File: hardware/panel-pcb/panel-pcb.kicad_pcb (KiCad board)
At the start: 4 copper layers, 135.5 x 127 mm, 131 parts, among them J1 USB_C_Receptacle_USB2.0_16P, J10 RS-485 OUT, J11 12V_OUT, J2 SWD, J3 FSR North, J4 FSR East, J5 12V_IN, J6 FSR South, J7 FSR West, J8 RS-485 IN, J9 INT OUT, SW1 PANEL_ID, SW2 BOOTSEL, SW3 RS-485 Termination, U1 RP2040, U2 THVD1419, U3 W25Q32JV, U4 SN74AHCT125, U5 AMS1117-5.0, U6 AP7361C-33ER-13, U7 USBLC6-2SC6, X1 12MHz

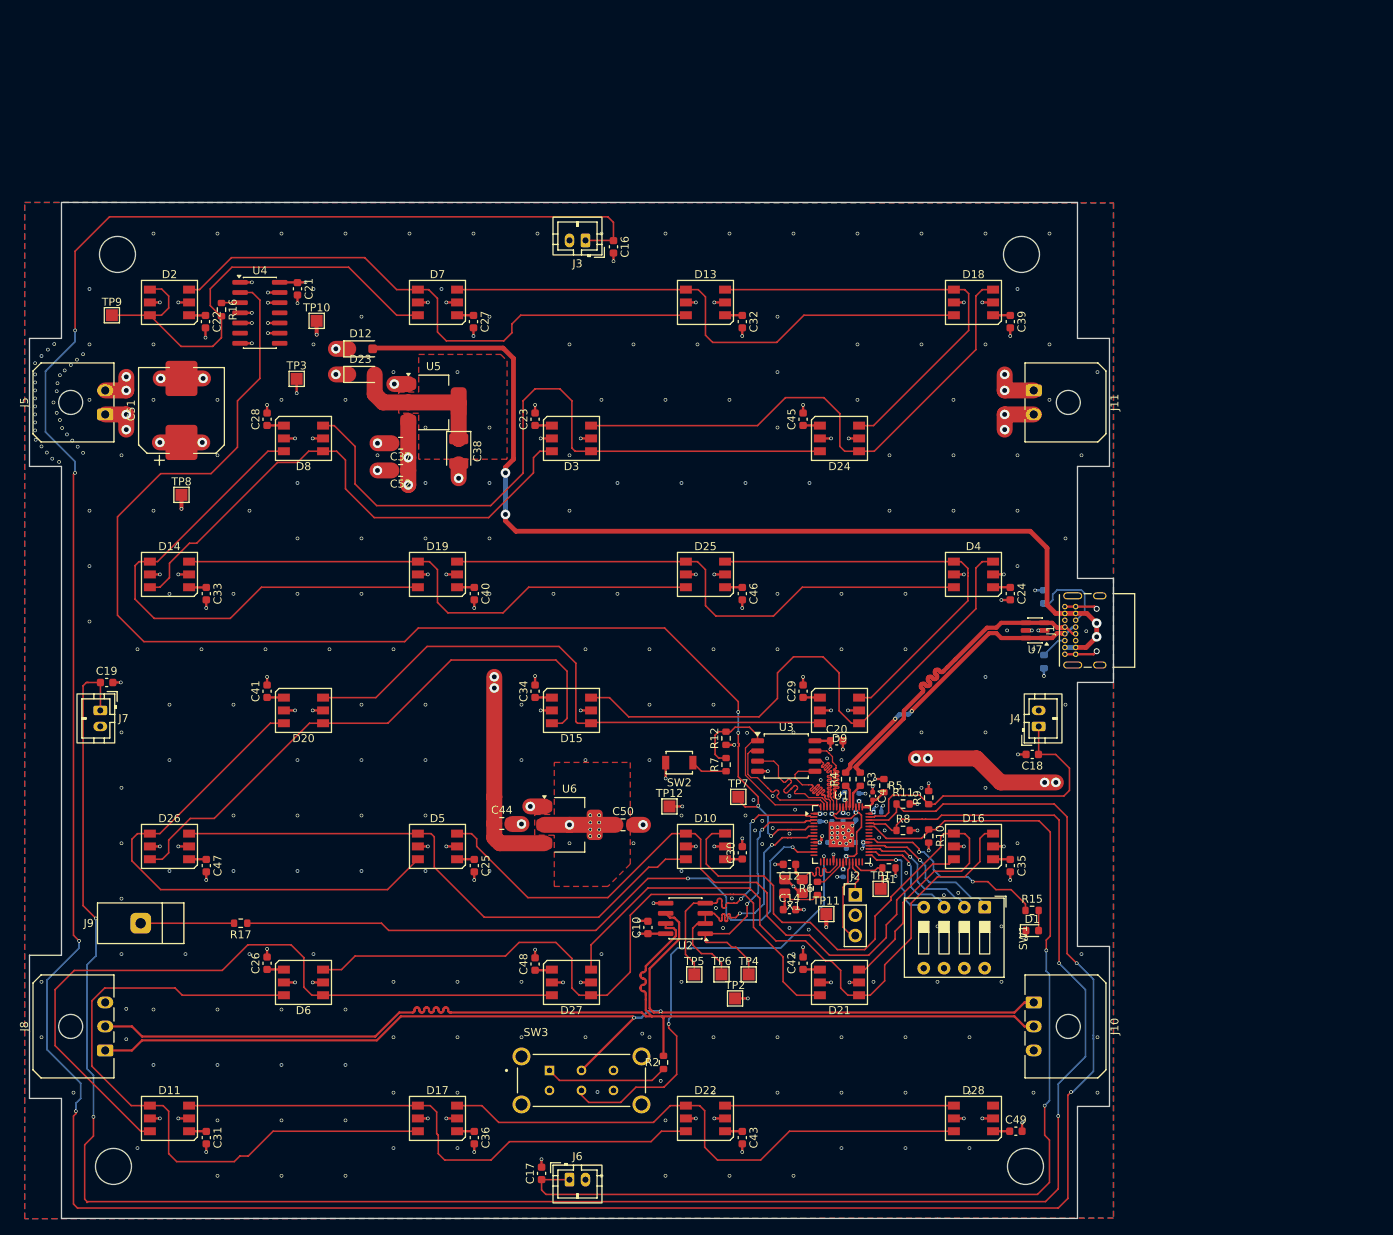
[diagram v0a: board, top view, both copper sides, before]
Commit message: Panel PCB: silkscreen positioning pass, verified ERC/DRC exclusions, page settings
- Reposition reference/value silkscreen across the board.
- Fix J1 B1/B12 starved thermal spokes.
- Save C51's edited electrolytic footprint into panel-pcb.pretty as
  CP_Elec_10x10.5_RVT1E471M and re-associate.
- Exclude verified-benign warnings: 25 lib_footprint_mismatch DRC
  false positives (rotation-correlated, content identical to library)
  and lib_symbol_mismatch ERC noise (cached flattened copies of
  derived library symbols, pins verified identical).
- Page settings: A3 -> A4 landscape, title block date/rev refreshed,
  stale mounting-hole placeholder comment removed.

Still pending before fab: silkscreen additions (name/rev/logos/JLC
order-number placeholder), final gerber export.
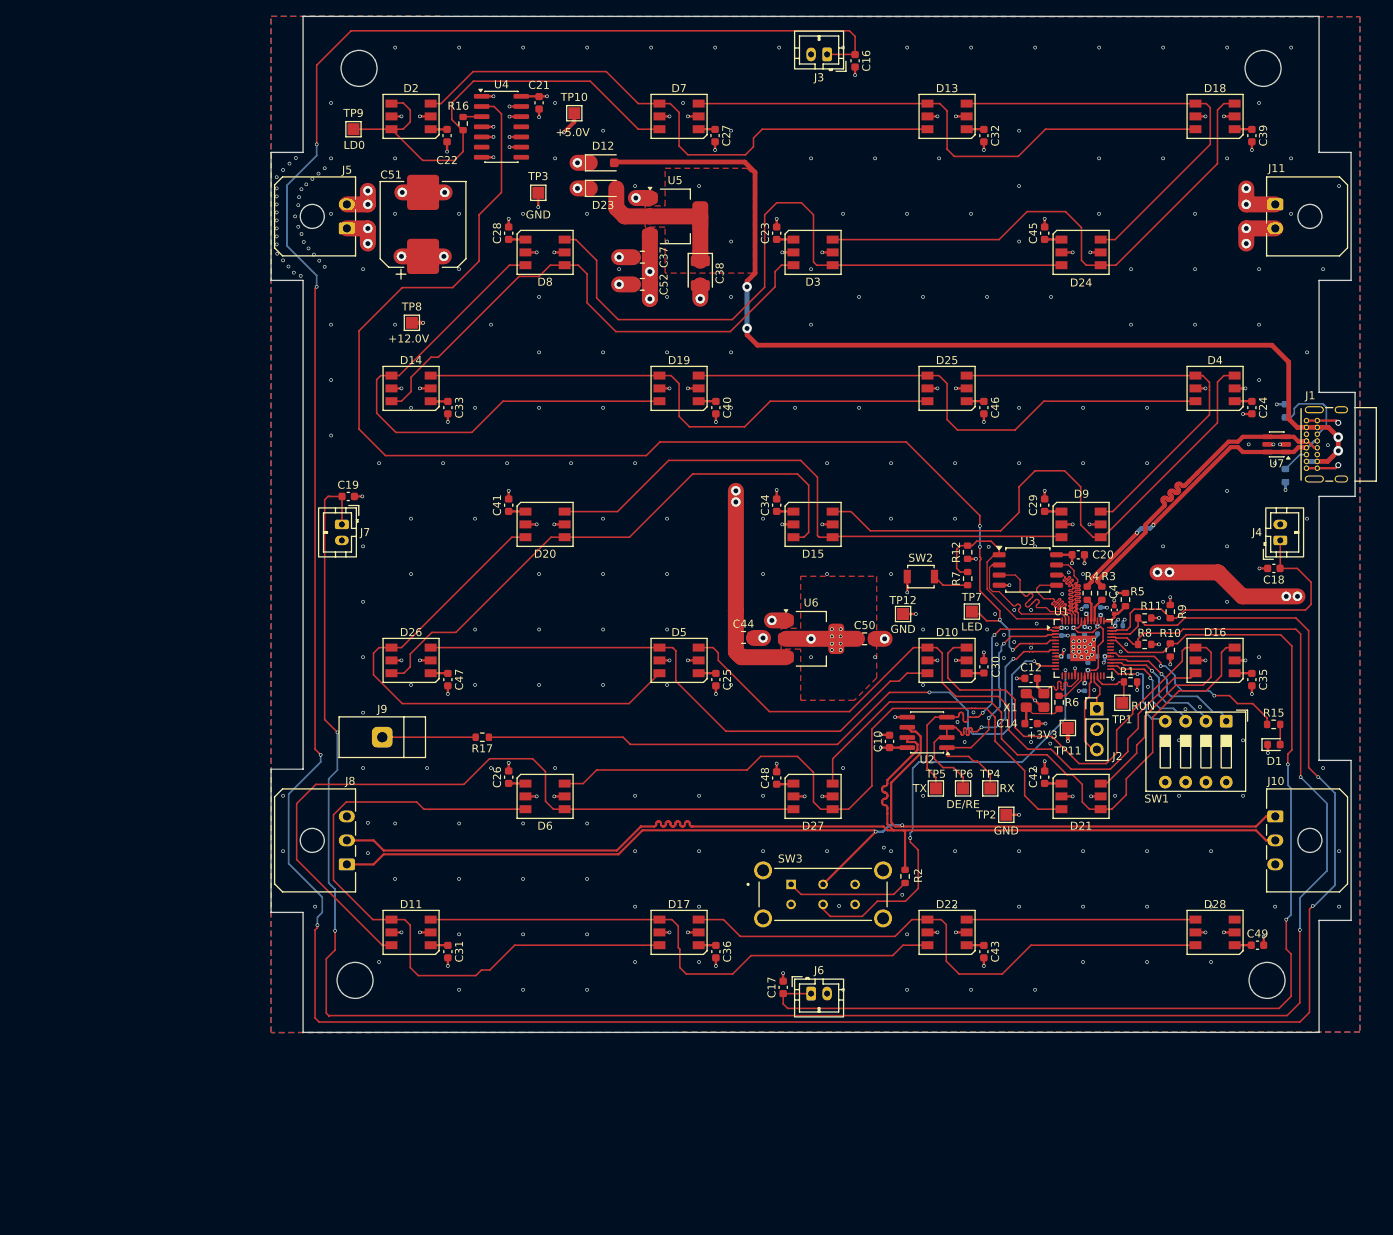
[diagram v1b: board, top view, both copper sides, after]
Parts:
- C51: footprint Capacitor_SMD:CP_Elec_10x10.5 -> panel-pcb:CP_Elec_10x10.5_RVT1E471M
- moved TP10 41.4 mm to (114.1, 38.8)
- moved TP2 40.9 mm to (168.1, 126.5)
- moved C10 38.1 mm to (153.5, 117.4)
- moved C24 38.1 mm to (198.8, 75.6)
- moved C25 38.1 mm to (131.8, 109.6)
- moved C30 38.1 mm to (165.3, 108.0)
- moved C35 38.1 mm to (198.8, 109.6)
- moved C40 38.1 mm to (131.8, 75.6)
- moved C46 38.1 mm to (165.3, 75.6)
- moved D1 38.1 mm to (201.6, 117.8)
- moved R11 38.1 mm to (185.4, 101.9)
- moved R7 38.1 mm to (163.3, 97.0)
- moved SW2 38.1 mm to (157.4, 96.8)
- moved U3 38.1 mm to (170.8, 95.9)
- moved C32 38.1 mm to (165.3, 41.6)
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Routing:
- net +5.0V: track 34.7 -> 35.9 mm
- net Net-(D23-A): track 17.9 -> 18.9 mm
- net GPIO3: track 164.6 -> 165.3 mm
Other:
- outline, holes or cut-outs redrawn

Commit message: Panel PCB: design-review batch 2 - first-BIN ground, 12V sense divider, QSPI margin
- D2.6 (first WS2815 BIN) rewired from /LD0 to GND, matching the
  vendor application circuit (review finding P3-2; the old BOM.md
  claim that the datasheet ties it to the data source was wrong).
- New 12V presence sense: R18 100k from +12.0V, R19 22k to GND,
  C53 100nF filter, midpoint to GPIO17 (U1.28). ~2.16V at 12V,
  ~100uA injection ceiling into an unpowered GPIO. Lets firmware
  gate LED data output on 12V-good so USB-only bench power never
  drives unpowered WS2815 inputs (review finding P4-2).
- QSPI_SD0/SD2 pinch widened 0.09mm -> 0.127mm (was at JLC's
  absolute multilayer minimum spacing; review finding P5-06).
- Board recentered on the new A4 sheet; zones refilled.

ERC 0 errors; DRC 0 violations, 0 unconnected.
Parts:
- added C53: 100nF X7R 50V, Capacitor_SMD:C_0603_1608Metric, F.Cu at (196.4, 89.8)
- added R18: 100k, Resistor_SMD:R_0603_1608Metric, F.Cu at (193.8, 89.1)
- added R19: 22k, Resistor_SMD:R_0603_1608Metric, F.Cu at (193.8, 93.1)
- R12: value 10k DNF -> 10k
- X1: value 12MHz -> 12MHz ABM8-272-T3
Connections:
- D2 pad 6: /LD0 -> GND
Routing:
- net GPIO17: track 0.00 -> 31.7 mm, vias 0 -> 2
- net GND: track 144.1 -> 147.5 mm, vias 391 -> 394
- net +12.0V: track 59.0 -> 60.0 mm, vias 34 -> 35
- net /LD0: track 59.0 -> 58.3 mm
